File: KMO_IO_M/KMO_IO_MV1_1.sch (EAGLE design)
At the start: 66 parts, among them Q1 8MHz, Q2 25MHz, U1 ATMEGA328

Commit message: IO BL rev
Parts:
- added D1, D2: M7, SparkFun-DiscreteSemi:DIODESMA
- added IC1, IC2, IC3, IC4, IC5, IC6, IC7: 100p, SparkFun-Passives:CAP0805
- added ID1, ID2, ID3, ID4, ID5, ID6, ID7: 3V3, diode:ZENER-DIODESOT23
- added IIR1, IIR2, IIR3, IIR4, IIR5, IIR6, IIR7: 22, SparkFun-Passives:RESISTOR0805-RES
- added OL1, OL2, OL3: YLW, led:LEDCHIP-LED0805
- added OLR1, OLR2, OLR3: 330, SparkFun-Passives:RESISTOR0805-RES
- INDL: value BLUE -> BLU
- PL: value RED -> GRN
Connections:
- new net A10: IC4.1, ID4.C, IIR4.1
- new net A11: IC5.1, ID5.C, IIR5.1
- new net A12: IC6.1, ID6.C, IIR6.1
- new net A13: IC7.1, ID7.C, IIR7.1
- new net A8: IC2.1, ID2.C, IIR2.1
- new net A9: IC3.1, ID3.C, IIR3.1
- new net BLG: BL-6.S, C1.1, D2.A, INDL.C, Q1.2, SR.S, U1.AGND, U1.GND@1, U1.GND@2
- new net BLV: BL-2.S, C3.2, D1.C, R1.2, R2.2, R3.2, U1.AVCC, U1.VCC@1, U1.VCC@2
- new net N$12: IIR1.2, XI-4.1
- new net N$20: IIR2.2, XI-5.1
- new net N$21: IIR3.2, XI-6.1
- new net N$23: IIR4.2, XI-7.1
- new net N$25: IIR5.2, XI-8.1
- new net N$26: IIR6.2, XI-9.1
- new net N$27: IIR7.2, XI-10.1
- new net N$6: OL3.A, OLR3.1
- new net N$7: OL1.A, OLR1.1
- new net N$8: OL2.A, OLR2.1
- net +3V3: now also D1.A; no longer BL-2.S, C3.2, R1.2, R2.2, R3.2, U1.AVCC, U1.VCC@1, U1.VCC@2
- net A1: now also IC1.1, ID1.C, IIR1.1; no longer XI-4.1
- net A2: no longer XI-5.1
- net A3: no longer XI-6.1
- net A4: no longer XI-7.1
- net A5: no longer XI-8.1
- net A6: no longer XI-9.1
- net A7: no longer XI-10.1
- net D5: now also OLR3.2
- net D6: now also OLR2.2
- net D7: now also OLR1.2
- net GND: now also D2.C, IC1.2, IC2.2, IC3.2, IC4.2, IC5.2, IC6.2, IC7.2, ID1.A, ID2.A, ID3.A, ID4.A, ID5.A, ID6.A, ID7.A, OL1.C, OL2.C, OL3.C; no longer BL-6.S, C1.1, INDL.C, Q1.2, SR.S, U1.AGND, U1.GND@1, U1.GND@2
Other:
- note added: "-> V5"
- note removed: "-> V3.3"
- moved on the sheet: INDL, IR1, IR2, IR3, IR4, IR5, IR6, IR7, OD1, OD2, OD3, OQ1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

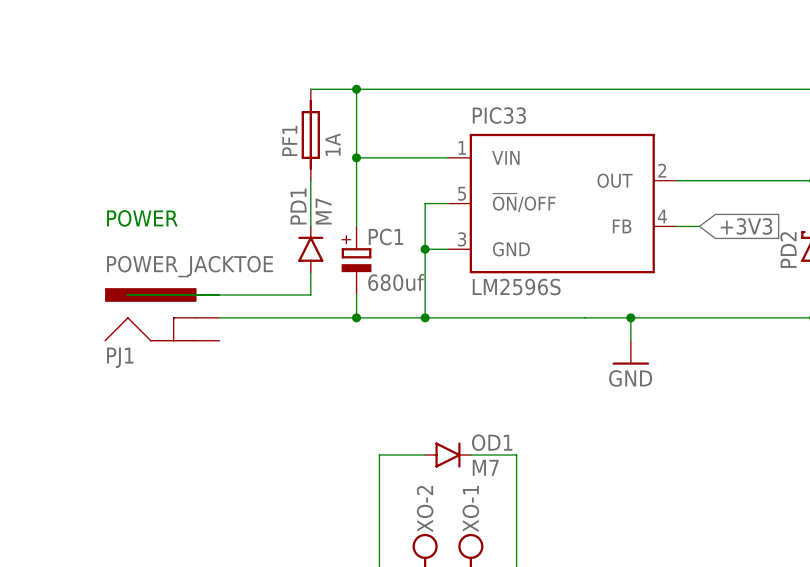
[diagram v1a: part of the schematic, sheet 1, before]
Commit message: 1.1 inductance value rev
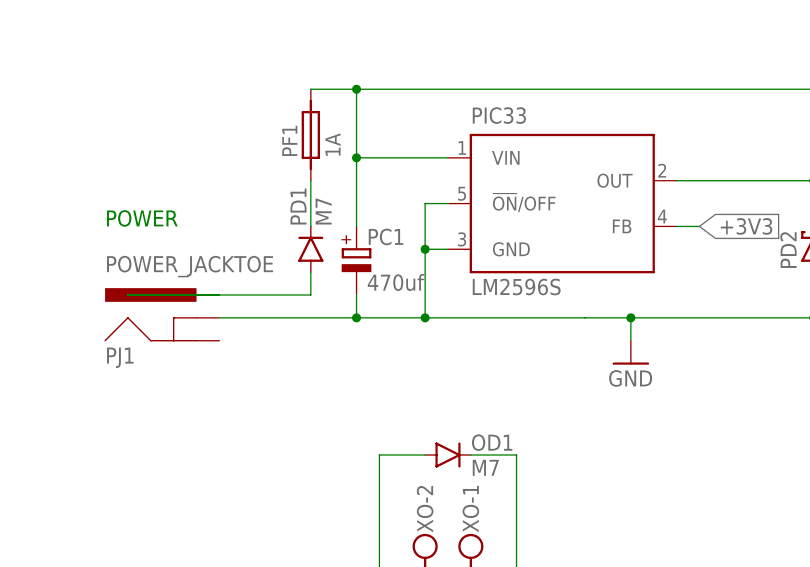
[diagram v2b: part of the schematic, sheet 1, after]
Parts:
- PC1: value 680uf -> 470uf
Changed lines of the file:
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@@
 <part name="Q1" library="Testing" deviceset="RESONATOR" device="1:1" value="8MHz"/>
 <part name="R3" library="SparkFun-Passives" deviceset="RESISTOR" device="0805-RES"/>
-<part name="PC1" library="rcl" library_urn="urn:adsk.eagle:library:334" deviceset="CPOL-EU" device="140CLH-1010" package3d_urn="urn:adsk.eagle:package:23391/1" value="680uf"/>
+<part name="PC1" library="rcl" library_urn="urn:adsk.eagle:library:334" deviceset="CPOL-EU" device="140CLH-1010" package3d_urn="urn:adsk.eagle:package:23391/1" value="470uf"/>
 <part name="PC2" library="rcl" library_urn="urn:adsk.eagle:library:334" deviceset="CPOL-EU" device="140CLH-1010" package3d_urn="urn:adsk.eagle:package:23391/1" value="220uf"/>
 <part name="PCO" library="inductor-coilcraft" deviceset="MSS1260" device="" value="33 uh"/>

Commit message: out led rev
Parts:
- removed OLR1, OLR2, OLR3: 330, SparkFun-Passives:RESISTOR0805-RES
- PR1: value 470 -> 1k
- R6: value 330 -> 1k
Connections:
- net BLG: now also C3.2
- net BLV: now also C3.1; no longer C3.2
- net D5: no longer OLR3.2
- net D6: no longer OLR2.2
- net D7: no longer OLR1.2
- net GND: no longer C3.1, OR1.1, OR2.1, OR3.1
- net N$6: now also OR3.1; no longer OLR3.1
- net N$7: now also OL2.A, OR2.1; no longer OL1.A, OLR1.1
- net N$8: now also OL1.A, OR1.1; no longer OL2.A, OLR2.1
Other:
- moved on the sheet: C2, C3, D2, OL1, OL2, OL3, OR1, OR2, OR3, R2, SR

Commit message: al con
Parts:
- PC1: value 470uf -> 470uf 25v
- PC2: value 220uf -> 220uf 50v
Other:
- note added: "Optional"
- moved on the sheet: PC1, PC2, PD1, PF1, PJ1

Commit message: 11 ok
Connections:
- net D11: now also BL-4.S, U1.PB3(MOSI/OC2); no longer BL-1.S, U1.PB4(MISO)
- net D12: now also BL-1.S, U1.PB4(MISO); no longer BL-4.S, U1.PB3(MOSI/OC2)
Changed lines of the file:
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@@
 </segment>
 <segment>
-<wire x1="114.3" y1="22.86" x2="116.84" y2="22.86" width="0.1524" layer="91"/>
-<pinref part="U1" gate="G$1" pin="PB4(MISO)"/>
-<label x="116.84" y="22.86" size="1.27" layer="95" xref="yes"/>
-</segment>
-<segment>
-<wire x1="149.86" y1="45.72" x2="147.32" y2="45.72" width="0.1524" layer="91"/>
-<label x="147.32" y="45.72" size="1.778" layer="95" rot="R180" xref="yes"/>
-<pinref part="BL" gate="-1" pin="S"/>
+<pinref part="U1" gate="G$1" pin="PB3(MOSI/OC2)"/>
+<wire x1="114.3" y1="25.4" x2="116.84" y2="25.4" width="0.1524" layer="91"/>
+<label x="116.84" y="25.4" size="1.27" layer="95" xref="yes"/>
+</segment>
+<segment>
+<pinref part="BL" gate="-4" pin="S"/>
+<wire x1="149.86" y1="50.8" x2="147.32" y2="50.8" width="0.1524" layer="91"/>
+<label x="147.32" y="50.8" size="1.778" layer="95" rot="R180" xref="yes"/>
 </segment>
 </net>
@@
 </segment>
 <segment>
-<wire x1="114.3" y1="25.4" x2="116.84" y2="25.4" width="0.1524" layer="91"/>
-<pinref part="U1" gate="G$1" pin="PB3(MOSI/OC2)"/>
-<label x="116.84" y="25.4" size="1.27" layer="95" xref="yes"/>
-</segment>
-<segment>
-<wire x1="149.86" y1="50.8" x2="147.32" y2="50.8" width="0.1524" layer="91"/>
-<label x="147.32" y="50.8" size="1.778" layer="95" rot="R180" xref="yes"/>
-<pinref part="BL" gate="-4" pin="S"/>
-</segment>
-</net>
+<pinref part="U1" gate="G$1" pin="PB4(MISO)"/>
+<wire x1="114.3" y1="22.86" x2="116.84" y2="22.86" width="0.1524" layer="91"/>
+<label x="116.84" y="22.86" size="1.27" layer="95" xref="yes"/>
+</segment>
+<segment>
+<pinref part="BL" gate="-1" pin="S"/>
+<wire x1="149.86" y1="45.72" x2="147.32" y2="45.72" width="0.1524" layer="91"/>
+<label x="147.32" y="45.72" size="1.778" layer="95" rot="R180" xref="yes"/>
+</segment>
+</net>
